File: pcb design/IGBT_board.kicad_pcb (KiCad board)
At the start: 4 copper layers, 162 x 100 mm, 266 parts, among them J2 DESAT, J3 DESAT, J4 PHASE, Q1 IGBT, Q10 IGBT, Q11 IGBT, Q12 IGBT, Q13 NPN, Q14 PNP, Q15 CSD19533Q5A, Q16 CSD19533Q5A, Q17 NPN, Q18 PNP, Q19 PNP, Q2 IGBT, Q20 PNP, Q3 IGBT, Q4 IGBT, Q5 IGBT, Q6 IGBT, Q7 IGBT, Q8 IGBT, Q9 IGBT, T1 TRANS-3-1CT, U1 ISO5852S, U10 AMC1200, U11 TLP2745, U12 OPA2172, U13 LM3480, U14 LM3480, U2 LM5030, U3 ISO5852S, U4 NAND, U5 APE8865U5-33-HF-3, U6 NAND, U7 NAND, U8 TLP2745, U9 OPA2172

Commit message: Changed power supply from 15/-8V to +15/-15V se we can make better use uf programmable -VEE. Changed connector to 14pos. Connected some missing signals. Updated layout
Signed-off-by: Marcos Chaparro <mchaparro@paltatech.com>
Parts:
- removed C53, C54: 100nF, IPC7351-Nominal:CAPC1608X55
- removed the REF** at (-51.9, 46.1)
- removed U4, U6, U7: NAND, smd-semi:SOT-23-5
- added D20: 1N4148W, smd-semi:SOD-123, F.Cu at (51.5, 36.3)
- added D21: GSOT03C, smd-semi:SOT-23, F.Cu at (51.5, 33.1)
- added J1: 61001421121, paltatech:conn-2x7-2.54mm_SMD, F.Cu at (-45.4, 45.0)
- added R93: 330R, IPC7351-Nominal:RESC1608X50, F.Cu at (-38.9, 33.0)
- added R94: 330R, IPC7351-Nominal:RESC1608X50, F.Cu at (36.4, 33.0)
- C50: value 100nF -> 100pF
- D15: value BAT54S -> 1N4148W; footprint smd-semi:SOT-23 -> smd-semi:SOD-123
- D17: value BAT54S -> GSOT03C
- U11, U8: value TLP2745 -> SI8710B
- moved U8 192.7 mm to (-37.6, 25.0), turned to 90 degrees
- moved C82 187.2 mm to (-50.0, 38.7), turned to 270 degrees
- moved D17 183.6 mm to (-126.9, 85.8), turned to 90 degrees
- moved C77 176.7 mm to (-45.5, 38.7), turned to 270 degrees
- moved D15 96.6 mm to (-123.7, 77.7)
- moved R28 96.6 mm to (-123.7, 75.0)
- moved TP3 96.6 mm to (-122.2, 80.5)
- moved C46 96.6 mm to (-114.5, 72.7)
- moved C8 96.6 mm to (-115.3, 70.5)
- moved R25 96.6 mm to (-118.3, 72.0)
- moved R26 96.6 mm to (-118.3, 73.6)
- moved R27 96.6 mm to (-116.0, 72.7)
- moved TP4 96.6 mm to (-126.2, 80.2)
- moved J2 88.9 mm to (-91.0, 11.4)
- moved D4 88.0 mm to (-91.0, 5.75)
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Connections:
- C50 pad 1: 3.3v -> /SYNC
- C50 pad 2: GND -> Net-(C50-Pad2)
- C77 pad 1: /IN_BOTTOM -> /PWM_N
- C82 pad 1: /IN_TOP -> /PWM_P
- D15 pad 1: GND -> /FAULT
- D15 pad 2: 3.3v -> /PWM_P
- D17 pad 1: GND -> /PWM_P
- D17 pad 2: 3.3v -> /PWM_N
- D17 pad 3: /IN_BOTTOM -> GND
- R28 pad 1: /IN_TOP -> /PWM_N
- R35 pad 1: Net-(R35-Pad1) -> Net-(C50-Pad2)
- R45 pad 1: /IN_BOTTOM -> /PWM_P
- R54 pad 2: /IN_BOTTOM -> /PWM_N
- R59 pad 1: /IN_TOP -> /PWM_P
- TP13 pad 1: /IN_BOTTOM -> /PWM_N
- TP3 pad 1: /IN_TOP -> /PWM_P
- U1 pad 10: /FAULT -> /PWM_P
- U1 pad 11: Net-(U1-Pad11) -> /PWM_N
- U10 pad 6: /phase voltage/Vout- -> /V_phase-
- U10 pad 7: /phase voltage/Vout+ -> /V_phase+
- U2 pad 9: Net-(R35-Pad1) -> Net-(C50-Pad2)
- U3 pad 10: /FAULT -> /PWM_N
- U3 pad 11: Net-(U3-Pad11) -> /PWM_P
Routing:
- net GATE_LOW: track 539.8 -> 1003.4 mm, vias 43 -> 58
- net VBUS-: track 693.6 -> 239.2 mm, vias 76 -> 63
- net 3.3v: track 158.7 -> 36.6 mm, vias 8 -> 11
- net 24v: track 42.8 -> 163.6 mm, vias 0 -> 16
- net /IN_BOTTOM: track 106.4 -> 0.00 mm
- net /PWM_N: track 0.00 -> 92.8 mm
- net /PWM_P: track 0.00 -> 92.3 mm, vias 0 -> 1
- net /VEE_CTRL: track 0.00 -> 87.8 mm
- net /FAULT: track 153.9 -> 73.0 mm, vias 12 -> 4
- net /RESET: track 133.9 -> 53.0 mm, vias 2 -> 0
- net /V_phase+: track 0.00 -> 71.0 mm
- net /V_phase-: track 0.00 -> 70.5 mm
- net (no net): track 4.28 -> 72.5 mm, vias 4 -> 10
- net /PWR_GOOD: track 130.1 -> 65.4 mm, vias 2 -> 0
- net Net-(C16-Pad1): track 40.7 -> 7.06 mm, vias 2 -> 0
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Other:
- outline, holes or cut-outs redrawn

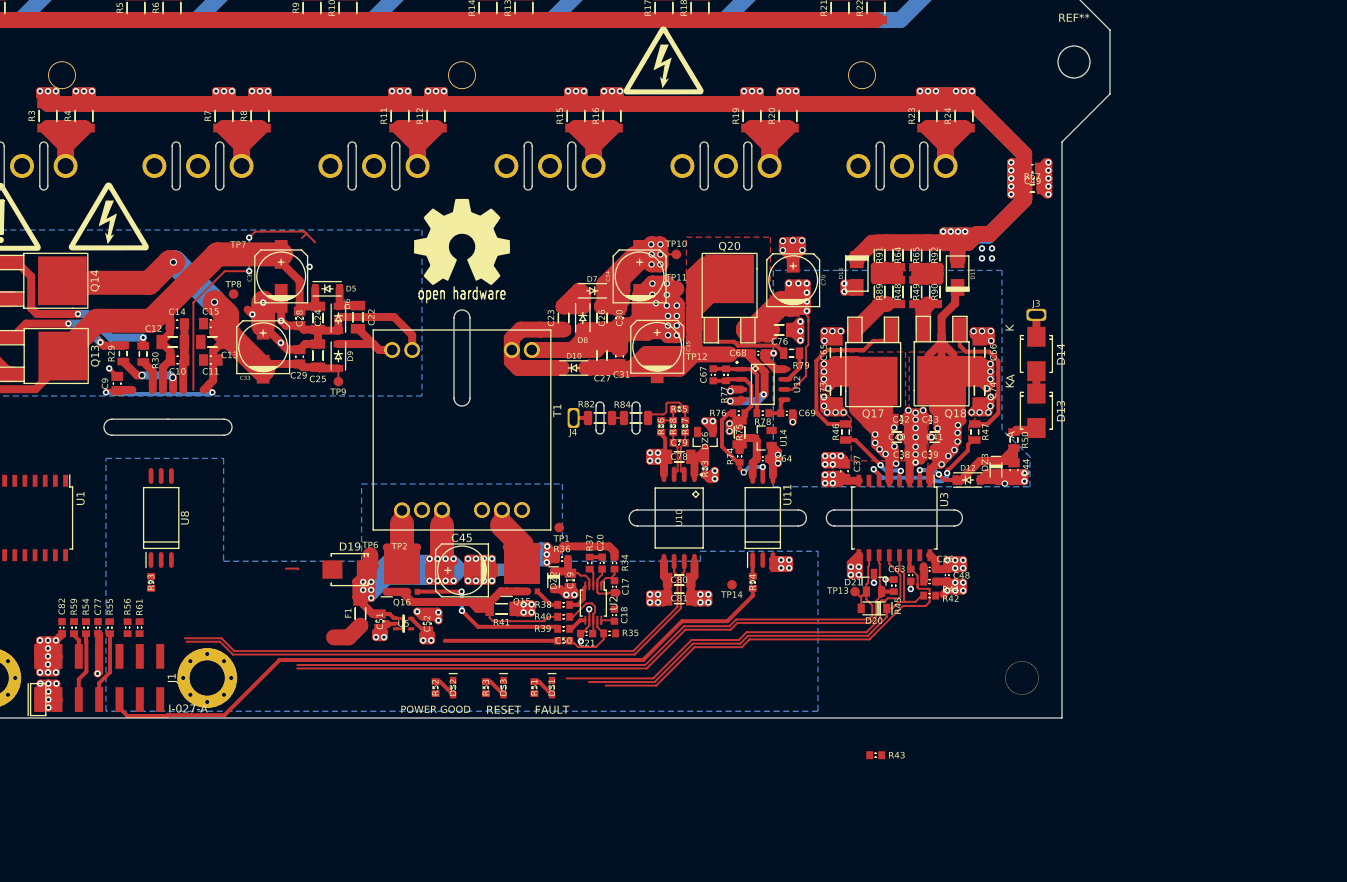
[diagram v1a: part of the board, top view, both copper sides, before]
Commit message: Changed isolated amplifier from AMC1200 to AMC1301 because it has reinforced isolation. This required a different layout
Signed-off-by: Marcos Chaparro <mchaparro@paltatech.com>
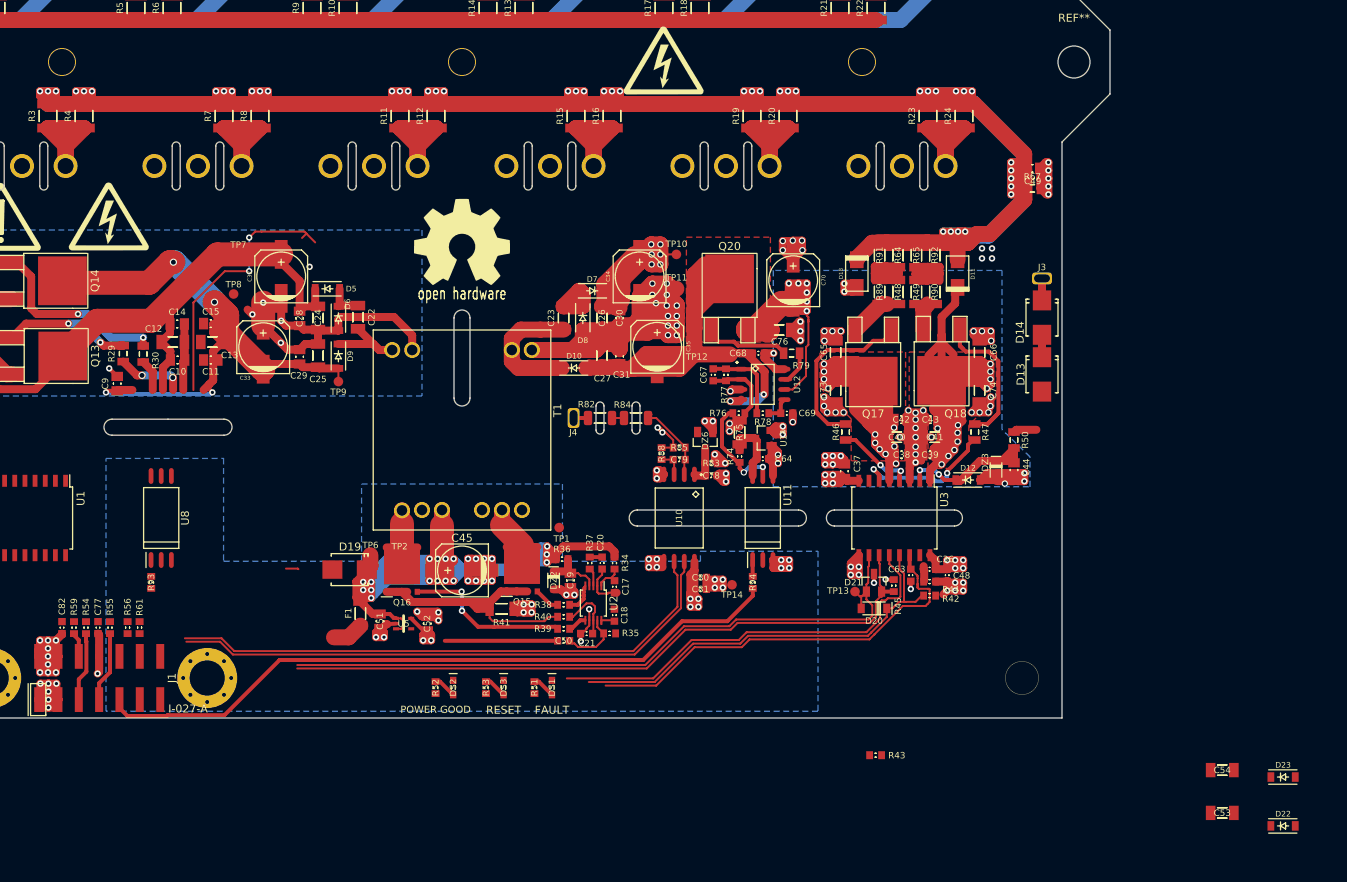
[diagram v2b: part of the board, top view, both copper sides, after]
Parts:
- removed R86: 10k, IPC7351-Nominal:RESC1608X50
- removed R87: 12R, IPC7351-Nominal:RESC1608X50
- added C53: 10uF 50v, IPC7351-Nominal:CAPC3216X70, F.Cu at (95.0, 61.9)
- added C54: 10uF 50v, IPC7351-Nominal:CAPC3216X70, F.Cu at (95.0, 56.5)
- added D22: RB160MM-60TR, paltatech:SOD-123F, F.Cu at (102.6, 63.5)
- added D23: RB160MM-60TR, paltatech:SOD-123F, F.Cu at (102.6, 57.4)
- C78, C80: footprint IPC7351-Nominal:CAPC3216X70 -> IPC7351-Nominal:CAPC1608X55
- C81: value 1uF -> 2.2uF; footprint IPC7351-Nominal:CAPC3216X70 -> IPC7351-Nominal:CAPC1608X55
- R68, R74: value 380R -> 390R
- R88: value 12R -> 1k
- R93, R94: value 330R -> 390R
- TP12, TP9: value -8v -> -15v
- U10: value AMC1200 -> AMC1301
- moved R85 4.80 mm to (27.1, 16.2)
- moved C78 4.64 mm to (31.1, 19.7), turned to 180 degrees
- moved D13 4.60 mm to (72.5, 7.05)
- moved D14 4.60 mm to (72.5, -0.05)
- moved J3 4.60 mm to (72.5, -4.95)
- moved R88 3.70 mm to (24.9, 16.9)
- moved C81 2.89 mm to (29.8, 33.9), turned to 0 degrees
- moved C80 2.67 mm to (29.8, 32.5), turned to 0 degrees
- moved C79 2.10 mm to (27.1, 17.7)
- moved MP1 1.65 mm to (0.00, -32.0)
- moved R83 1.03 mm to (31.1, 18.1), turned to 0 degrees
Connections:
- C25 pad 2: /IGBT_driver_TOP/-8V -> /IGBT_driver_TOP/-15V
- C27 pad 2: /IGBT_driver_BOT/-8V -> /IGBT_driver_BOT/-15V
- C29 pad 2: /IGBT_driver_TOP/-8V -> /IGBT_driver_TOP/-15V
- C31 pad 2: /IGBT_driver_BOT/-8V -> /IGBT_driver_BOT/-15V
- C33 pad 2: /IGBT_driver_TOP/-8V -> /IGBT_driver_TOP/-15V
- C35 pad 2: /IGBT_driver_BOT/-8V -> /IGBT_driver_BOT/-15V
- C60 pad 1: /IGBT_driver_TOP/-8V -> /IGBT_driver_TOP/-15V
- C68 pad 1: /IGBT_driver_BOT/-8V -> /IGBT_driver_BOT/-15V
- D10 pad 1: Net-(C23-Pad2) -> VBUS-
- D10 pad 2: /IGBT_driver_BOT/-8V -> Net-(C54-Pad1)
- D9 pad 1: Net-(C22-Pad2) -> PHASE
- D9 pad 2: /IGBT_driver_TOP/-8V -> Net-(C53-Pad1)
- Q19 pad 2: /IGBT_driver_TOP/-8V -> /IGBT_driver_TOP/-15V
- Q20 pad 2: /IGBT_driver_BOT/-8V -> /IGBT_driver_BOT/-15V
- R84 pad 1: Net-(R84-Pad1) -> /phase voltage/VIN+
- R85 pad 1: Net-(R84-Pad1) -> /phase voltage/VIN+
- R85 pad 2: Net-(R85-Pad2) -> VBUS-
- R88 pad 1: Net-(R85-Pad2) -> VBUS-
- TP12 pad 1: /IGBT_driver_BOT/-8V -> /IGBT_driver_BOT/-15V
- TP9 pad 1: /IGBT_driver_TOP/-8V -> /IGBT_driver_TOP/-15V
- U12 pad 4: /IGBT_driver_BOT/-8V -> /IGBT_driver_BOT/-15V
- U9 pad 4: /IGBT_driver_TOP/-8V -> /IGBT_driver_TOP/-15V
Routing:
- net VBUS-: track 239.2 -> 688.7 mm, vias 63 -> 78
- net GATE_LOW: track 1003.4 -> 561.5 mm, vias 58 -> 45
- net /IGBT_driver_BOT/-8V: track 66.4 -> 0.00 mm, vias 2 -> 0
- net /IGBT_driver_BOT/-15V: track 0.00 -> 64.4 mm, vias 0 -> 2
- net /IGBT_driver_TOP/-8V: track 46.6 -> 0.00 mm, vias 2 -> 0
- net /IGBT_driver_TOP/-15V: track 0.00 -> 24.6 mm
- net /IGBT_driver_TOP/-VEE: track 46.5 -> 66.8 mm, vias 2 -> 4
- net Net-(R84-Pad1): track 7.82 -> 0.00 mm
- net Net-(C23-Pad2): track 16.4 -> 11.0 mm
- net Net-(C22-Pad2): track 10.8 -> 5.37 mm
- net PHASE: track 285.8 -> 291.2 mm
- net /phase voltage/VIN+: track 5.66 -> 10.3 mm
- net /IGBT_driver_BOT/+15V: track 109.3 -> 113.7 mm, vias 22 -> 24
- net 3.3v: track 36.6 -> 40.6 mm
- net Net-(C78-Pad2): track 8.32 -> 4.66 mm
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
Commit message: More .step 3D models included for better portability
Signed-off-by: Marcos Chaparro <mchaparro@paltatech.com>
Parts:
- moved C55 296.6 mm to (-114.8, 5.47)
- moved C56 296.6 mm to (-130.2, 22.4)
- moved C57 296.6 mm to (-144.8, 21.7)
- moved C58 296.6 mm to (-137.0, 15.1)
- moved C59 296.6 mm to (-123.5, -14.7)
- moved C60 296.6 mm to (-117.0, -19.7)
- moved C61 296.6 mm to (-125.1, -8.12)
- moved C62 296.6 mm to (-132.6, -16.2)
- moved C71 296.6 mm to (-129.3, 5.90)
- moved C72 296.6 mm to (-129.3, 11.2)
- moved C75 296.6 mm to (-144.8, -3.41)
- moved C83 296.6 mm to (-122.5, 11.7)
- moved Q19 296.6 mm to (-143.6, -9.31)
- moved R62 296.6 mm to (-163.0, -11.6)
- moved R63 296.6 mm to (-163.0, -4.60)
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- renumbered REF** to eREF**
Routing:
- net Net-(Q17-Pad3): track 5.35 -> 13.9 mm
- net Net-(Q18-Pad3): track 3.38 -> 9.65 mm
- net GATE_LOW: track 561.5 -> 566.1 mm
- net /IGBT_driver_BOT/+15V: track 113.7 -> 117.9 mm
- net Net-(R32-Pad1): track 5.54 -> 1.70 mm, vias 2 -> 0
- net Net-(D13-Pad2): track 2.91 -> 6.65 mm
- net /IGBT_driver_BOT/supply control/PWM: track 13.3 -> 15.9 mm
- net /IGBT_driver_BOT/-VEE: track 116.3 -> 118.6 mm
- net VBUS-: track 688.7 -> 690.8 mm, vias 78 -> 80
- net Net-(R48-Pad1): track 13.9 -> 11.8 mm
- net /IGBT_driver_BOT/12.0V: track 5.00 -> 6.74 mm
- net Net-(R49-Pad1): track 11.0 -> 11.7 mm
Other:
- outline, holes or cut-outs redrawn

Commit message: Larger 2512 gate resistors
Signed-off-by: Marcos Chaparro <mchaparro@paltatech.com>
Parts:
- removed R57, R58, R64, R65: 2R, IPC7351-Nominal:RESC3216X60
- removed R80, R81, R91, R92: NI, IPC7351-Nominal:RESC3216X60
- R31, R32, R48, R49, R69, R75, R89, R90: footprint IPC7351-Nominal:RESC3216X60 -> IPC7351-Nominal:RESC6432X70
- moved C53 196.7 mm to (-99.0, 29.4)
- moved C54 196.7 mm to (-99.0, 24.1)
- moved D22 196.7 mm to (-91.4, 31.0)
- moved D23 196.7 mm to (-91.4, 24.9)
- moved R48 4.83 mm to (49.8, -4.35)
- moved R49 4.78 mm to (61.5, -4.35)
- moved D18 3.00 mm to (46.6, -4.35)
- moved D11 2.95 mm to (64.7, -4.35)
- moved R90 1.86 mm to (57.6, -4.35)
- moved R89 1.82 mm to (53.6, -4.35)
- moved C70 0.90 mm to (41.6, -4.72)
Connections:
- R31 pad 1: Net-(R31-Pad1) -> GATE_HIGH
- R32 pad 1: Net-(R32-Pad1) -> GATE_HIGH
- R48 pad 1: Net-(R48-Pad1) -> GATE_LOW
- R49 pad 1: Net-(R49-Pad1) -> GATE_LOW
- R69 pad 1: Net-(R31-Pad1) -> GATE_HIGH
- R75 pad 1: Net-(R32-Pad1) -> GATE_HIGH
- R89 pad 1: Net-(R48-Pad1) -> GATE_LOW
- R90 pad 1: Net-(R49-Pad1) -> GATE_LOW
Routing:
- net GATE_LOW: track 566.1 -> 595.5 mm, vias 45 -> 48
- net Net-(R48-Pad1): track 11.8 -> 0.00 mm
- net Net-(R49-Pad1): track 11.7 -> 0.00 mm
- net VBUS-: track 690.8 -> 697.0 mm
- net Net-(Q14-Pad3): track 8.33 -> 4.90 mm
- net Net-(Q13-Pad3): track 10.2 -> 13.7 mm
- net GATE_HIGH: track 167.9 -> 171.3 mm
- net 3.3v: track 40.6 -> 43.4 mm
- net Net-(C36-Pad1): track 1.89 -> 3.84 mm
- net Net-(Q18-Pad3): track 9.65 -> 11.6 mm
- net Net-(R32-Pad1): track 1.70 -> 0.00 mm
- net Net-(R31-Pad1): track 1.70 -> 0.00 mm
- net /IGBT_driver_BOT/-VEE: track 118.6 -> 117.2 mm, vias 21 -> 23
- net /IGBT_driver_BOT/-15V: track 64.4 -> 65.4 mm
- net Net-(Q17-Pad3): track 13.9 -> 13.3 mm
- added copper zone on F.Cu, net /IGBT_driver_BOT/-15V
- added copper zone on PWR.Cu, net 3.3v
- added copper zone on GNDs.Cu, net GND
- removed copper zone on F.Cu, net /IGBT_driver_BOT/-8V
- removed copper zone on B.Cu, net GND

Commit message: Added current sensor connector. Layout is now symmetrical
Signed-off-by: Marcos Chaparro <mchaparro@paltatech.com>
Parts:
- removed the G*** at (-44.1, -12.7)
- removed the G*** at (-57.6, -12.7)
- removed HOLE102 (x2): MOUNTING_HOLE, paltatech:SMD_STANDOFF_M3
- removed R55: 22R, IPC7351-Nominal:RESC1608X50
- removed the REF** at (0.00, 50.0)
- added C85: 1uF, IPC7351-Nominal:CAPC1608X55, F.Cu at (63.3, 42.2)
- added J5: PHASE CURRENT CONN, paltatech:TE-292227-4, F.Cu at (71.8, 40.0)
- added R57: 1k, IPC7351-Nominal:RESC1608X50, F.Cu at (49.0, 34.0)
- added R58: 1k, IPC7351-Nominal:RESC1608X50, F.Cu at (-59.0, 33.7)
- J1: value 61001421121 -> CONN-100MIL-M-2x8; footprint paltatech:conn-2x7-2.54mm_SMD -> conn-100mil:CONN-100MIL-M-2x8
- R31, R32, R48, R49: value 2R -> 3R
- U5: value APE8865U5-33-HF-3 -> LM1117IMP-v.v; footprint SC-70-5 -> smd-semi:SOT-223
- moved R66 207.9 mm to (21.8, 77.9)
- moved R62 195.5 mm to (10.9, 77.9)
- moved R63 195.5 mm to (10.9, 84.9)
- moved DS4 193.5 mm to (-11.3, 97.5)
- moved R26 152.5 mm to (34.2, 76.7), turned to 0 degrees
- moved C54 113.8 mm to (13.8, 8.45), turned to 180 degrees
- moved U13 113.1 mm to (-31.6, 15.0)
- moved Q19 112.1 mm to (-31.6, -6.70), turned to 180 degrees
- moved D23 111.3 mm to (18.6, 8.40)
- moved C75 106.6 mm to (-38.2, 1.50)
- moved U9 100.9 mm to (-33.5, 8.30)
- moved C56 96.9 mm to (-33.5, 17.6)
- moved C61 96.8 mm to (-30.4, 11.9), turned to 180 degrees
- moved R73 96.4 mm to (-29.9, 4.25), turned to 180 degrees
- moved C62 94.7 mm to (-38.5, -5.40), turned to 90 degrees
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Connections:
- C45 pad 1: 24v -> +24
- C46 pad 1: 3.3v -> +5
- C48 pad 1: 3.3v -> +5
- C51 pad 1: 24v -> +24
- C52 pad 1: 3.3v -> +5
- C80 pad 1: 3.3v -> +5
- C81 pad 1: 3.3v -> +5
- C82 pad 1: /PWM_P -> GND
- C82 pad 2: GND -> /PWM_P
- D19 pad 1: 24v -> +24
- F1 pad 1: 24v -> Net-(F1-Pad1)
- F1 pad 2: Net-(F1-Pad2) -> +24
- J1 pad 1: Net-(F1-Pad2) -> /I_phase-
- J1 pad 10: /SYNC -> GND
- J1 pad 13: /V_phase+ -> Net-(F1-Pad1)
- J1 pad 14: /V_phase- -> GND
- J1 pad 2: GND -> /I_phase+
- J1 pad 3: Net-(F1-Pad2) -> /V_phase-
- J1 pad 4: GND -> /V_phase+
- J1 pad 7: Net-(J1-Pad7) -> /VEE_CTRL
- J1 pad 8: GND -> /SYNC
- J1 pad 9: /VEE_CTRL -> /TEMP
- R25 pad 1: 3.3v -> +5
- R26 pad 1: 3.3v -> +5
- R27 pad 1: 3.3v -> +5
- R34 pad 2: 24v -> +24
- R36 pad 1: 24v -> +24
- R42 pad 1: 3.3v -> +5
- R43 pad 1: 3.3v -> +5
- R44 pad 1: 3.3v -> +5
- R51 pad 1: 3.3v -> +5
- R52 pad 1: 3.3v -> +5
- R53 pad 1: 3.3v -> +5
- R54 pad 1: Net-(J1-Pad5) -> Net-(J1-Pad12)
- R56 pad 1: Net-(J1-Pad11) -> /RESET
- R56 pad 2: /RESET -> Net-(J1-Pad5)
- R59 pad 1: /PWM_P -> Net-(J1-Pad11)
- R59 pad 2: Net-(J1-Pad6) -> /PWM_P
- R61 pad 1: /FAULT -> Net-(J1-Pad6)
- R61 pad 2: Net-(J1-Pad12) -> /FAULT
- T1 pad 13: PHASE -> Net-(C22-Pad2)
- T1 pad 14: Net-(C22-Pad2) -> PHASE
- T1 pad 3: 24v -> +24
- TP6 pad 1: 24v -> +24
- U10 pad 8: 3.3v -> +5
- U5 pad 1: 24v -> GND
- U5 pad 2: GND -> +5
- U5 pad 3: 24v -> +24
- U5 pad 4: Net-(U5-Pad4) -> +5
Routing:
- net GATE_HIGH: track 171.3 -> 618.4 mm, vias 0 -> 48
- net PHASE: track 291.2 -> 694.3 mm, vias 5 -> 70
- net +24: track 0.00 -> 194.5 mm, vias 0 -> 16
- net 24v: track 163.6 -> 0.00 mm, vias 16 -> 0
- net /RESET: track 53.0 -> 175.9 mm, vias 0 -> 6
- net /FAULT: track 73.0 -> 171.0 mm, vias 4 -> 6
- net /PWR_GOOD: track 65.4 -> 159.9 mm, vias 0 -> 6
- net /I_phase-: track 0.00 -> 94.0 mm, vias 0 -> 2
- net /I_phase+: track 0.00 -> 94.0 mm, vias 0 -> 2
- net (no net): track 72.5 -> 0.00 mm, vias 10 -> 1
- net /IGBT_driver_TOP/-VEE: track 66.8 -> 138.9 mm, vias 4 -> 25
- net /PWM_P: track 92.3 -> 159.7 mm, vias 1 -> 2
- net /PWM_N: track 92.8 -> 159.0 mm
- net +5: track 0.00 -> 57.5 mm, vias 0 -> 34
- net /IGBT_driver_TOP/-15V: track 24.6 -> 81.4 mm, vias 0 -> 18
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- added copper zone on F.Cu, net +5
- added copper zone on PWR.Cu, net +5
- added copper zone on F.Cu, net /IGBT_driver_TOP/+15V
- added copper zone on PWR.Cu, net /IGBT_driver_TOP/+15V
- added copper zone on B.Cu, net /IGBT_driver_TOP/-15V
- added copper zone on F.Cu, net /IGBT_driver_TOP/-15V
- added copper zone on B.Cu, net /IGBT_driver_TOP/-VEE
- added copper zone on F.Cu, net /IGBT_driver_TOP/-VEE
- added copper zone on GNDs.Cu, net PHASE
- removed copper zone on PWR.Cu, net 3.3v
- removed copper zone on B.Cu, net PHASE
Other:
- outline, holes or cut-outs redrawn
- board text added: "+15V"
- board text added: "-8V"
- board text added: "5V"
- board text added: "GND"
- board text added: "GND-H"
- board text added: "GND-L"
- board text added: "PWM-H"
- board text added: "PWM-L"
- board text added: "PWR GOOD"
- board text removed: "POWER GOOD"
